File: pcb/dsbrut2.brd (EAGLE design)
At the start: 51.6 x 38 mm, 14 parts, among them IC1 4175D, IC2 74HC125D, IC3 MEGA8-AI

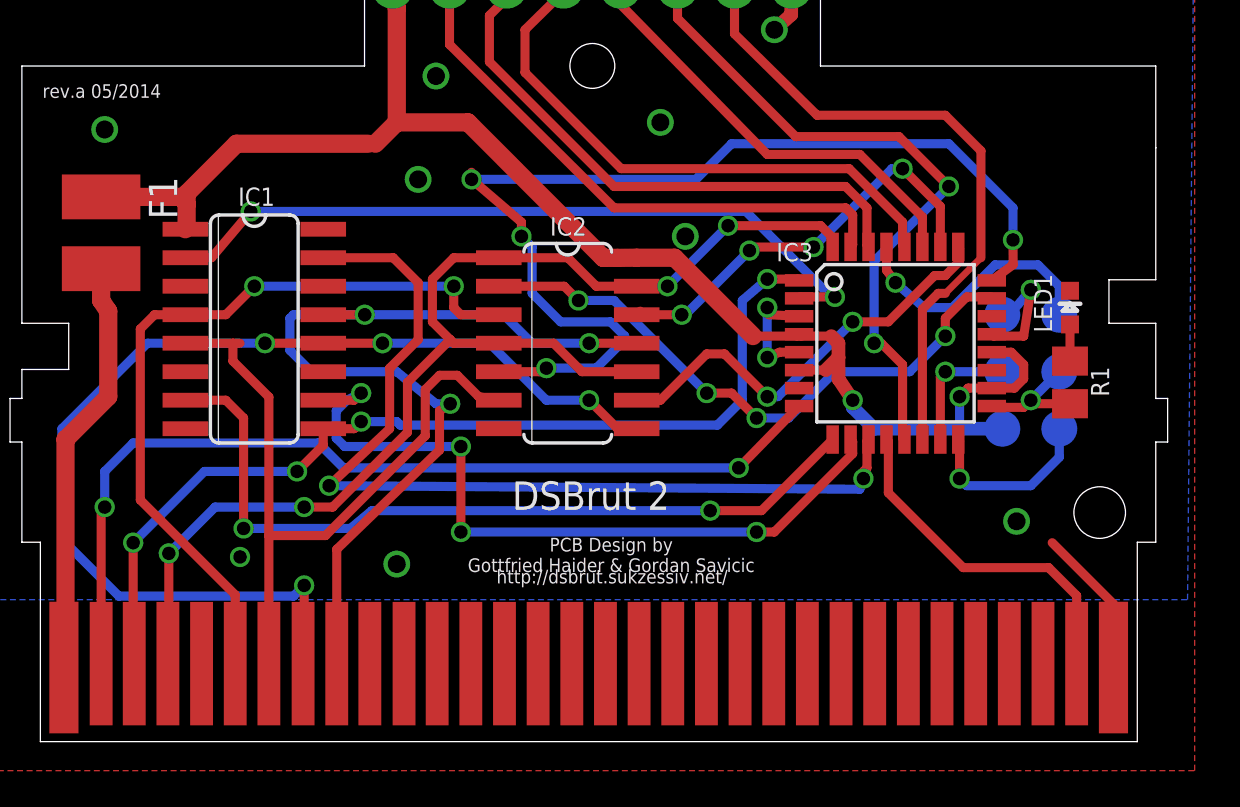
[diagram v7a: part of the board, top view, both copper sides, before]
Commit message: power supply pin 16 on ic1
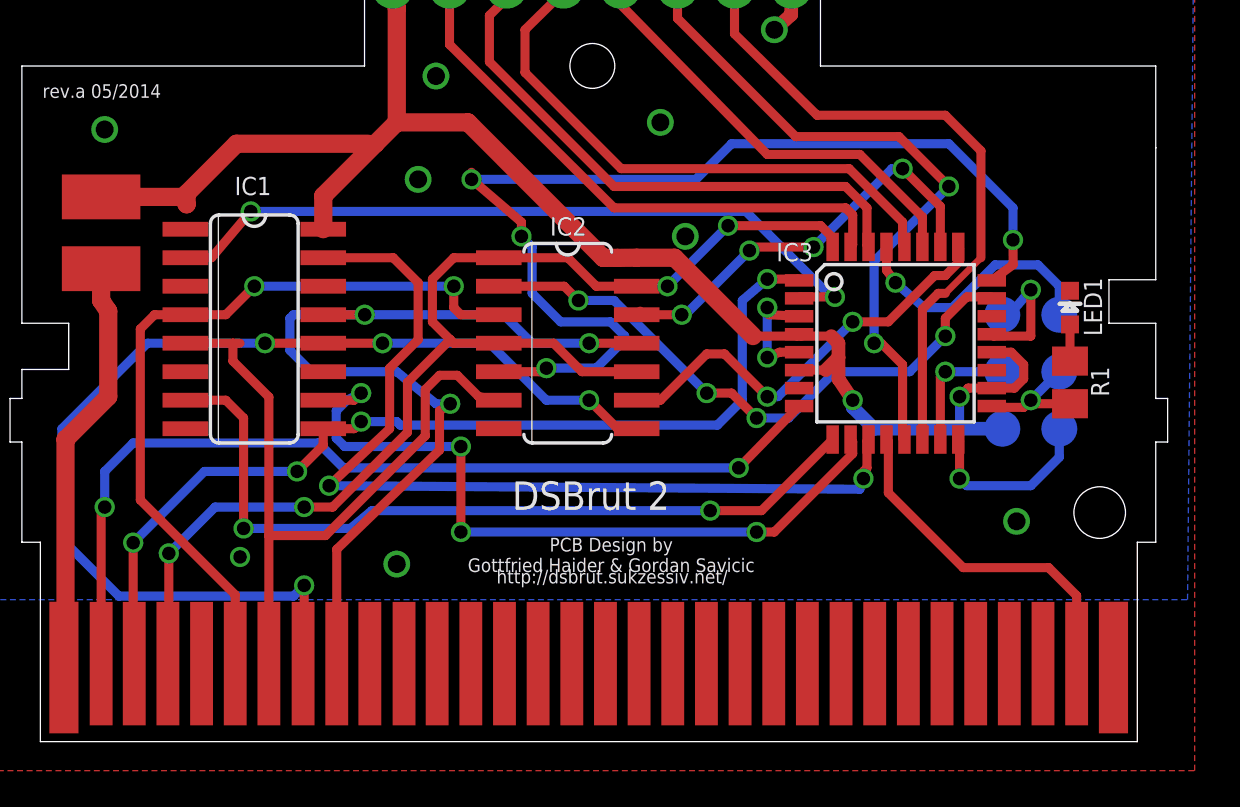
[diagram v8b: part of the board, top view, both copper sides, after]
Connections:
- removed net VDD: IC1.16
- net +3V3: now also IC1.16
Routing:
- net GND: track 20.5 -> 14.1 mm
- net +3V3: track 66.2 -> 69.8 mm
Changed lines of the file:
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@@
 <element name="IC1" library="40xx" package="SO16" value="4175D" x="9.525" y="18.415" smashed="yes" rot="R270">
 <attribute name="VALUE" x="8.255" y="17.0815" size="0.8128" layer="27" ratio="10" rot="R270"/>
-<attribute name="NAME" x="8.805228125" y="23.903928125" size="0.8128" layer="25" ratio="10"/>
+<attribute name="NAME" x="8.646478125" y="24.380178125" size="0.8128" layer="25" ratio="10"/>
 </element>
 <element name="IC2" library="74xx-eu" package="SO14" value="74HC125D" x="23.495" y="17.78" smashed="yes" rot="R270">
@@
 </element>
 <element name="LED1" library="SparkFunEagle-6-6-07" package="LED-0603" value="" x="45.87875" y="19.3675" smashed="yes">
-<attribute name="NAME" x="45.085" y="18.25625" size="0.8128" layer="25" rot="R90"/>
+<attribute name="NAME" x="47.3075" y="18.0975" size="0.8128" layer="25" rot="R90"/>
 <attribute name="VALUE" x="47.78375" y="18.7325" size="1.27" layer="27" rot="R90"/>
 </element>
@@
 </element>
 <element name="F1" library="dp_devices" package="L1812" value="F1" x="2.69875" y="22.70125" smashed="yes" rot="R270">
-<attribute name="NAME" x="4.82375" y="25.20125" size="1.27" layer="25" font="vector" ratio="10" rot="R270"/>
 <attribute name="VALUE" x="-0.04125" y="23.61375" size="0.8128" layer="27" font="vector" ratio="10" rot="R270"/>
 </element>
 </elements>
 <signals>
-<signal name="VDD">
-<contactref element="IC1" pad="16"/>
-</signal>
 <signal name="GND">
 <contactref element="IC2" pad="7"/>
@@
 <via x="44.1325" y="20.16125" extent="1-16" drill="0.6"/>
 <wire x1="42.4751" y1="18.0975" x2="42.3926" y2="18.18" width="0.4064" layer="1"/>
-<wire x1="47.8156375" y1="3.32515" x2="47.8156375" y2="6.1593625" width="0.4064" layer="1"/>
-<wire x1="47.8156375" y1="6.1593625" x2="45.085" y2="8.89" width="0.4064" layer="1"/>
 <via x="16.8275" y="25.0825" extent="1-16" drill="0.8"/>
 <via x="28.73375" y="22.5425" extent="1-16" drill="0.8"/>
@@
 <wire x1="32.7025" y1="31.75" x2="33.45308125" y2="32.419734375" width="0.6096" layer="1"/>
 <wire x1="33.45308125" y1="32.419734375" x2="33.466540625" y2="34.56710625" width="0.6096" layer="1"/>
-<wire x1="42.4751" y1="18.0975" x2="43.815" y2="18.0975" width="0.4064" layer="1"/>
-<wire x1="43.815" y1="18.0975" x2="44.1325" y2="20.16125" width="0.4064" layer="1"/>
+<wire x1="42.4751" y1="18.0975" x2="44.1325" y2="18.0975" width="0.4064" layer="1"/>
+<wire x1="44.1325" y1="18.0975" x2="44.1325" y2="20.16125" width="0.4064" layer="1"/>
 <contactref element="LED1" pad="C"/>
 <via x="43.4975" y="9.8425" extent="1-16" drill="0.8" diameter="0.8128"/>
@@
 <wire x1="8.73125" y1="26.67" x2="6.50875" y2="24.4475" width="0.8128" layer="1"/>
 <wire x1="6.50875" y1="24.4475" x2="6.50875" y2="23.97125" width="0.8128" layer="1"/>
-<wire x1="6.50875" y1="23.97125" x2="6.50875" y2="22.91715" width="0.8128" layer="1"/>
-<wire x1="6.50875" y1="22.91715" x2="6.4516" y2="22.86" width="0.8128" layer="1"/>
+<wire x1="6.50875" y1="23.97125" x2="6.50875" y2="22.91715" width="0" layer="19" extent="1-16"/>
+<wire x1="6.50875" y1="22.91715" x2="6.4516" y2="22.86" width="0" layer="19" extent="1-16"/>
 <wire x1="2.69875" y1="24.30125" x2="6.3625" y2="24.30125" width="0.8128" layer="1"/>
 <wire x1="6.3625" y1="24.30125" x2="6.50875" y2="23.97125" width="0.8128" layer="1"/>
+<contactref element="IC1" pad="16"/>
+<wire x1="12.5984" y1="22.86" x2="12.5984" y2="24.3459" width="0.8128" layer="1"/>
+<wire x1="12.5984" y1="24.3459" x2="14.9225" y2="26.67" width="0.8128" layer="1"/>
 </signal>
 <signal name="PD1">
